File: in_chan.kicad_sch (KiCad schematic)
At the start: 8 parts, among them U5 MAX31910AUI+

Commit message: fix most errors/warnings
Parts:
- renumbered C33 to C45, C34 to C46, C35 to C47, C36 to C48, R6 to R10, R7 to R11, U5 to U8
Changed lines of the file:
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@@
   (symbol (lib_id "power:GNDPWR") (at 163.83 119.38 0)
     (in_bom yes) (on_board yes) (fields_autoplaced)
-    (property "Reference" "#PWR031" (id 0) (at 163.83 124.46 0)
+    (property "Reference" "#PWR051" (id 0) (at 163.83 124.46 0)
       (effects (font (size 1.27 1.27)) hide)
     )
@@
   (symbol (lib_id "Device:R") (at 163.83 113.03 180)
     (in_bom yes) (on_board yes)
-    (property "Reference" "R7" (id 0) (at 166.37 111.76 0)
+    (property "Reference" "R11" (id 0) (at 166.37 111.76 0)
       (effects (font (size 1.27 1.27)) (justify right))
     )
@@
   (symbol (lib_id "power:GNDPWR") (at 204.47 151.13 0) (mirror y)
     (in_bom yes) (on_board yes) (fields_autoplaced)
-    (property "Reference" "#PWR032" (id 0) (at 204.47 156.21 0)
+    (property "Reference" "#PWR052" (id 0) (at 204.47 156.21 0)
       (effects (font (size 1.27 1.27)) hide)
     )
@@
   (symbol (lib_id "power:GNDPWR") (at 243.84 66.04 0)
     (in_bom yes) (on_board yes) (fields_autoplaced)
-    (property "Reference" "#PWR034" (id 0) (at 243.84 71.12 0)
+    (property "Reference" "#PWR054" (id 0) (at 243.84 71.12 0)
       (effects (font (size 1.27 1.27)) hide)
     )
@@
   (symbol (lib_id "Device:C") (at 243.84 62.23 0)
     (in_bom yes) (on_board yes)
-    (property "Reference" "C36" (id 0) (at 247.65 60.9599 0)
+    (property "Reference" "C48" (id 0) (at 247.65 60.9599 0)
       (effects (font (size 1.27 1.27)) (justify left))
     )
@@
   (symbol (lib_id "Maxim industrial IO:MAX31910AUI+") (at 204.47 143.51 0)
     (in_bom yes) (on_board yes) (fields_autoplaced)
-    (property "Reference" "U5" (id 0) (at 238.76 143.51 0)
+    (property "Reference" "U8" (id 0) (at 238.76 143.51 0)
       (effects (font (size 1.524 1.524)) (justify left))
     )
@@
   (symbol (lib_id "Device:C") (at 187.96 147.32 0) (mirror y)
     (in_bom yes) (on_board yes)
-    (property "Reference" "C33" (id 0) (at 184.15 146.0499 0)
+    (property "Reference" "C45" (id 0) (at 184.15 146.0499 0)
       (effects (font (size 1.27 1.27)) (justify left))
     )
@@
   (symbol (lib_id "power:GNDPWR") (at 219.71 87.63 0)
     (in_bom yes) (on_board yes) (fields_autoplaced)
-    (property "Reference" "#PWR033" (id 0) (at 219.71 92.71 0)
+    (property "Reference" "#PWR053" (id 0) (at 219.71 92.71 0)
       (effects (font (size 1.27 1.27)) hide)
     )
@@
   (symbol (lib_id "Device:C") (at 232.41 62.23 0)
     (in_bom yes) (on_board yes)
-    (property "Reference" "C35" (id 0) (at 236.22 60.9599 0)
+    (property "Reference" "C47" (id 0) (at 236.22 60.9599 0)
       (effects (font (size 1.27 1.27)) (justify left))
     )
@@
   (symbol (lib_id "power:GNDPWR") (at 160.02 73.66 270)
     (in_bom yes) (on_board yes)
-    (property "Reference" "#PWR030" (id 0) (at 154.94 73.66 0)
+    (property "Reference" "#PWR050" (id 0) (at 154.94 73.66 0)
       (effects (font (size 1.27 1.27)) hide)
     )
@@
   (symbol (lib_id "Device:C") (at 196.85 147.32 0) (mirror y)
     (in_bom yes) (on_board yes)
-    (property "Reference" "C34" (id 0) (at 193.04 146.0499 0)
+    (property "Reference" "C46" (id 0) (at 193.04 146.0499 0)
       (effects (font (size 1.27 1.27)) (justify left))
     )
@@
   (symbol (lib_id "Num-IO:4816P-T01-103LF") (at 153.67 80.01 0)
     (in_bom yes) (on_board yes)
-    (property "Reference" "R6" (id 0) (at 160.02 77.47 0)
+    (property "Reference" "R10" (id 0) (at 160.02 77.47 0)
       (effects (font (size 1.524 1.524)))
     )
@@
   (symbol (lib_id "Maxim industrial IO:MAX31910AUI+") (at 168.91 58.42 0)
     (in_bom yes) (on_board yes) (fields_autoplaced)
-    (property "Reference" "U5" (id 0) (at 194.31 46.99 0)
-      (effects (font (size 1.524 1.524)))
-    )
+    (property "Reference" "U8" (id 0) (at 194.31 46.99 0)
+      (effects (font (size 1.524 1.524)))
+    )

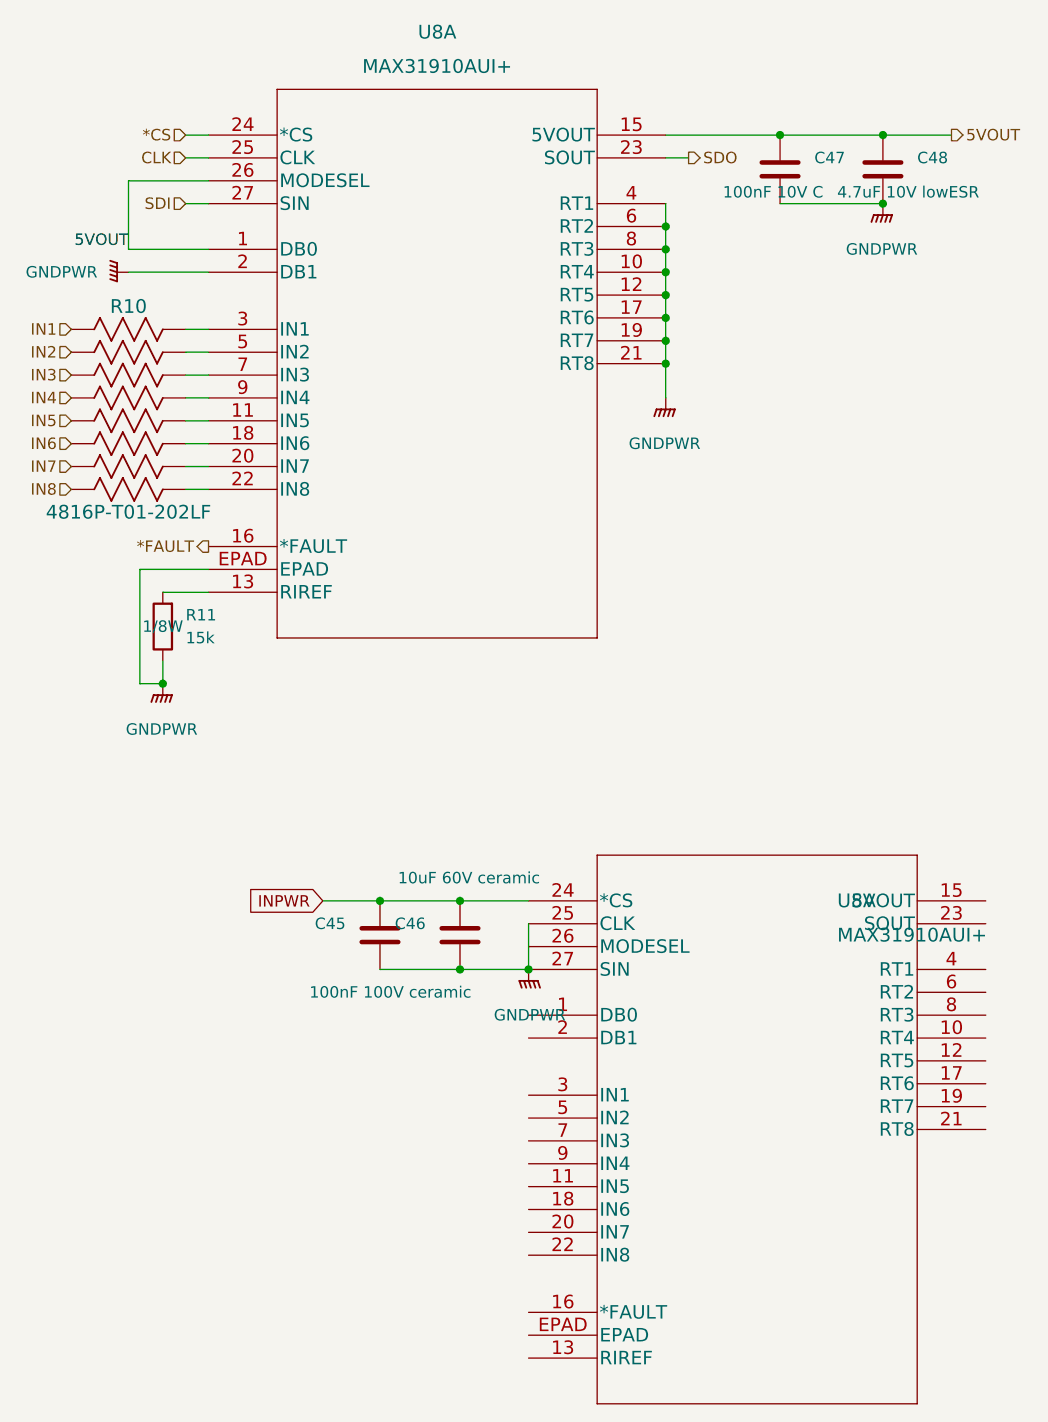
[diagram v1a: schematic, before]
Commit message: add KK connectors for power (check voltage or bypass)
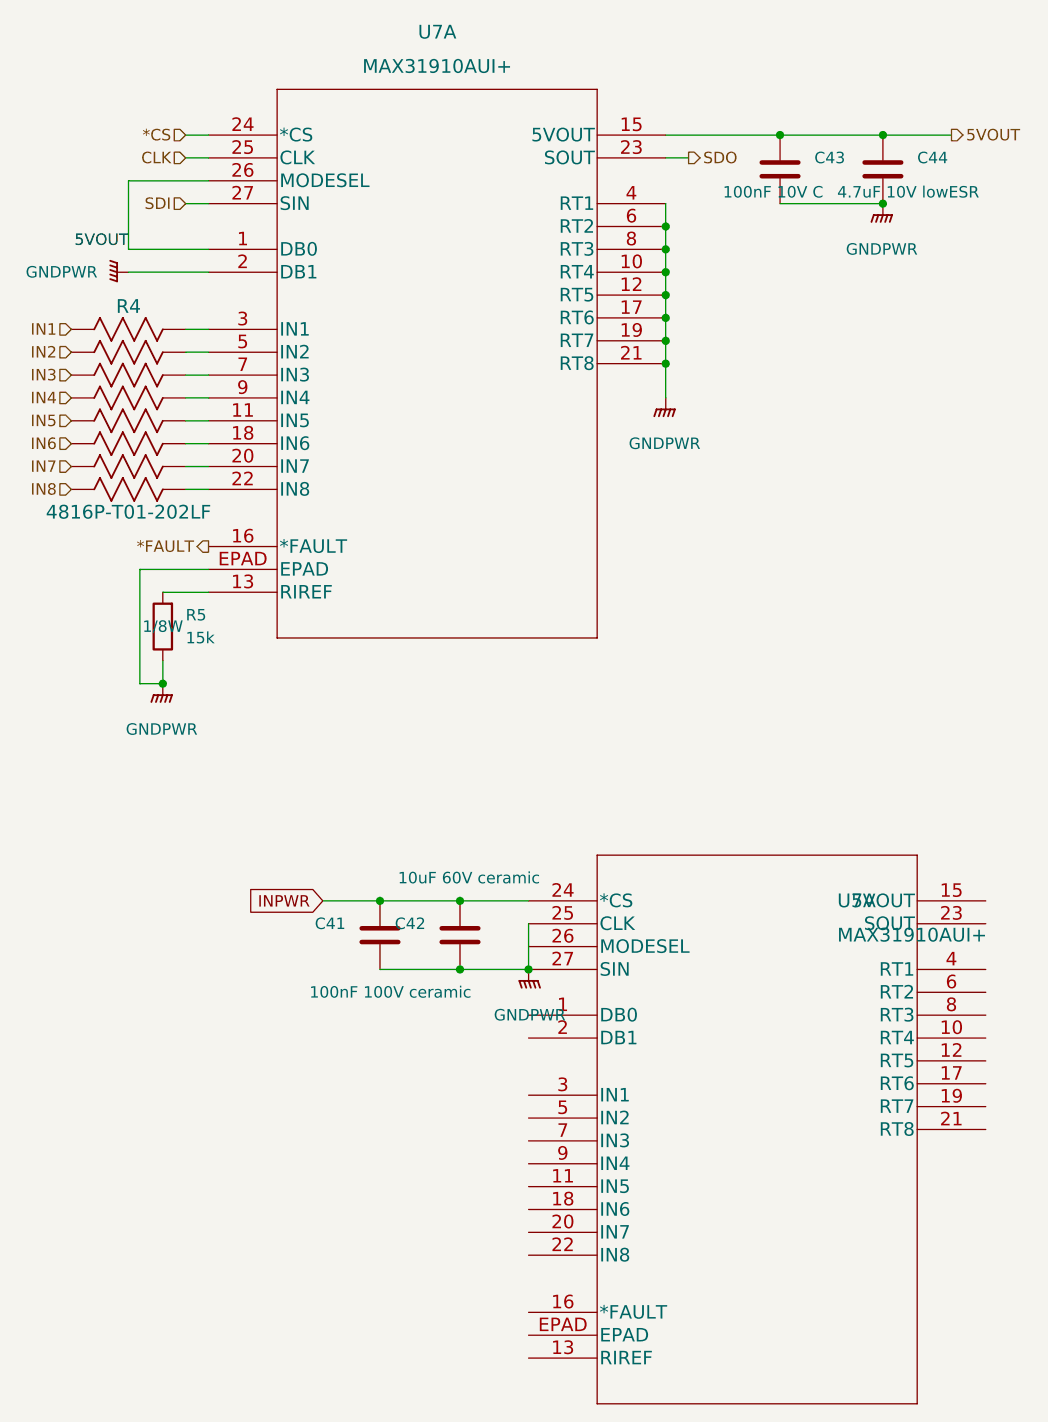
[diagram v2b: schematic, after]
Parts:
- renumbered C45 to C41, C46 to C42, C47 to C43, C48 to C44, R10 to R4, R11 to R5, U8 to U7
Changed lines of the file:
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@@
   (symbol (lib_id "Device:R") (at 163.83 113.03 180)
     (in_bom yes) (on_board yes)
-    (property "Reference" "R11" (id 0) (at 166.37 111.76 0)
+    (property "Reference" "R5" (id 0) (at 166.37 111.76 0)
       (effects (font (size 1.27 1.27)) (justify right))
     )
@@
   (symbol (lib_id "Device:C") (at 243.84 62.23 0)
     (in_bom yes) (on_board yes)
-    (property "Reference" "C48" (id 0) (at 247.65 60.9599 0)
+    (property "Reference" "C44" (id 0) (at 247.65 60.9599 0)
       (effects (font (size 1.27 1.27)) (justify left))
     )
@@
   (symbol (lib_id "Maxim industrial IO:MAX31910AUI+") (at 204.47 143.51 0)
     (in_bom yes) (on_board yes) (fields_autoplaced)
-    (property "Reference" "U8" (id 0) (at 238.76 143.51 0)
+    (property "Reference" "U7" (id 0) (at 238.76 143.51 0)
       (effects (font (size 1.524 1.524)) (justify left))
     )
@@
   (symbol (lib_id "Device:C") (at 187.96 147.32 0) (mirror y)
     (in_bom yes) (on_board yes)
-    (property "Reference" "C45" (id 0) (at 184.15 146.0499 0)
+    (property "Reference" "C41" (id 0) (at 184.15 146.0499 0)
       (effects (font (size 1.27 1.27)) (justify left))
     )
@@
   (symbol (lib_id "Device:C") (at 232.41 62.23 0)
     (in_bom yes) (on_board yes)
-    (property "Reference" "C47" (id 0) (at 236.22 60.9599 0)
+    (property "Reference" "C43" (id 0) (at 236.22 60.9599 0)
       (effects (font (size 1.27 1.27)) (justify left))
     )
@@
   (symbol (lib_id "Device:C") (at 196.85 147.32 0) (mirror y)
     (in_bom yes) (on_board yes)
-    (property "Reference" "C46" (id 0) (at 193.04 146.0499 0)
+    (property "Reference" "C42" (id 0) (at 193.04 146.0499 0)
       (effects (font (size 1.27 1.27)) (justify left))
     )
@@
   (symbol (lib_id "Num-IO:4816P-T01-103LF") (at 153.67 80.01 0)
     (in_bom yes) (on_board yes)
-    (property "Reference" "R10" (id 0) (at 160.02 77.47 0)
+    (property "Reference" "R4" (id 0) (at 160.02 77.47 0)
       (effects (font (size 1.524 1.524)))
     )
@@
   (symbol (lib_id "Maxim industrial IO:MAX31910AUI+") (at 168.91 58.42 0)
     (in_bom yes) (on_board yes) (fields_autoplaced)
-    (property "Reference" "U8" (id 0) (at 194.31 46.99 0)
+    (property "Reference" "U7" (id 0) (at 194.31 46.99 0)
       (effects (font (size 1.524 1.524)))
     )

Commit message: add resistances for bypassing the isolator
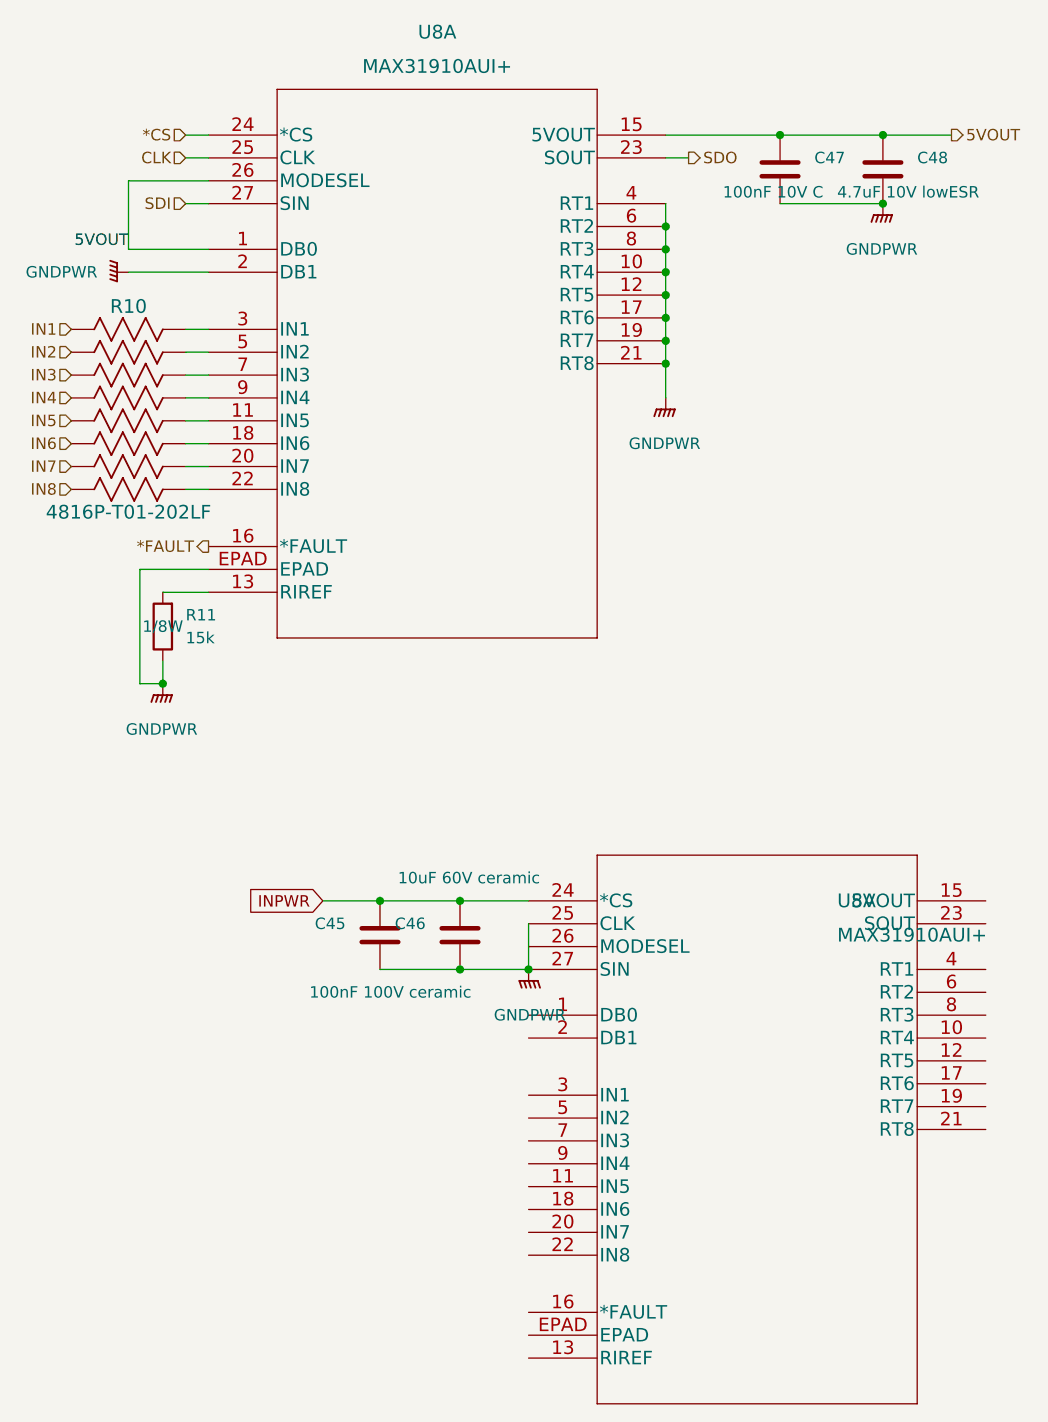
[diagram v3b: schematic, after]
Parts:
- renumbered C41 to C45, C42 to C46, C43 to C47, C44 to C48, R4 to R10, R5 to R11, U7 to U8
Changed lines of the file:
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@@
   (symbol (lib_id "Device:R") (at 163.83 113.03 180)
     (in_bom yes) (on_board yes)
-    (property "Reference" "R5" (id 0) (at 166.37 111.76 0)
+    (property "Reference" "R11" (id 0) (at 166.37 111.76 0)
       (effects (font (size 1.27 1.27)) (justify right))
     )
@@
   (symbol (lib_id "Device:C") (at 243.84 62.23 0)
     (in_bom yes) (on_board yes)
-    (property "Reference" "C44" (id 0) (at 247.65 60.9599 0)
+    (property "Reference" "C48" (id 0) (at 247.65 60.9599 0)
       (effects (font (size 1.27 1.27)) (justify left))
     )
@@
   (symbol (lib_id "Maxim industrial IO:MAX31910AUI+") (at 204.47 143.51 0)
     (in_bom yes) (on_board yes) (fields_autoplaced)
-    (property "Reference" "U7" (id 0) (at 238.76 143.51 0)
+    (property "Reference" "U8" (id 0) (at 238.76 143.51 0)
       (effects (font (size 1.524 1.524)) (justify left))
     )
@@
   (symbol (lib_id "Device:C") (at 187.96 147.32 0) (mirror y)
     (in_bom yes) (on_board yes)
-    (property "Reference" "C41" (id 0) (at 184.15 146.0499 0)
+    (property "Reference" "C45" (id 0) (at 184.15 146.0499 0)
       (effects (font (size 1.27 1.27)) (justify left))
     )
@@
   (symbol (lib_id "Device:C") (at 232.41 62.23 0)
     (in_bom yes) (on_board yes)
-    (property "Reference" "C43" (id 0) (at 236.22 60.9599 0)
+    (property "Reference" "C47" (id 0) (at 236.22 60.9599 0)
       (effects (font (size 1.27 1.27)) (justify left))
     )
@@
   (symbol (lib_id "Device:C") (at 196.85 147.32 0) (mirror y)
     (in_bom yes) (on_board yes)
-    (property "Reference" "C42" (id 0) (at 193.04 146.0499 0)
+    (property "Reference" "C46" (id 0) (at 193.04 146.0499 0)
       (effects (font (size 1.27 1.27)) (justify left))
     )
@@
   (symbol (lib_id "Num-IO:4816P-T01-103LF") (at 153.67 80.01 0)
     (in_bom yes) (on_board yes)
-    (property "Reference" "R4" (id 0) (at 160.02 77.47 0)
+    (property "Reference" "R10" (id 0) (at 160.02 77.47 0)
       (effects (font (size 1.524 1.524)))
     )
@@
   (symbol (lib_id "Maxim industrial IO:MAX31910AUI+") (at 168.91 58.42 0)
     (in_bom yes) (on_board yes) (fields_autoplaced)
-    (property "Reference" "U7" (id 0) (at 194.31 46.99 0)
+    (property "Reference" "U8" (id 0) (at 194.31 46.99 0)
       (effects (font (size 1.524 1.524)))
     )

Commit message: add condo for MPG isolator + small rerouting pair diff
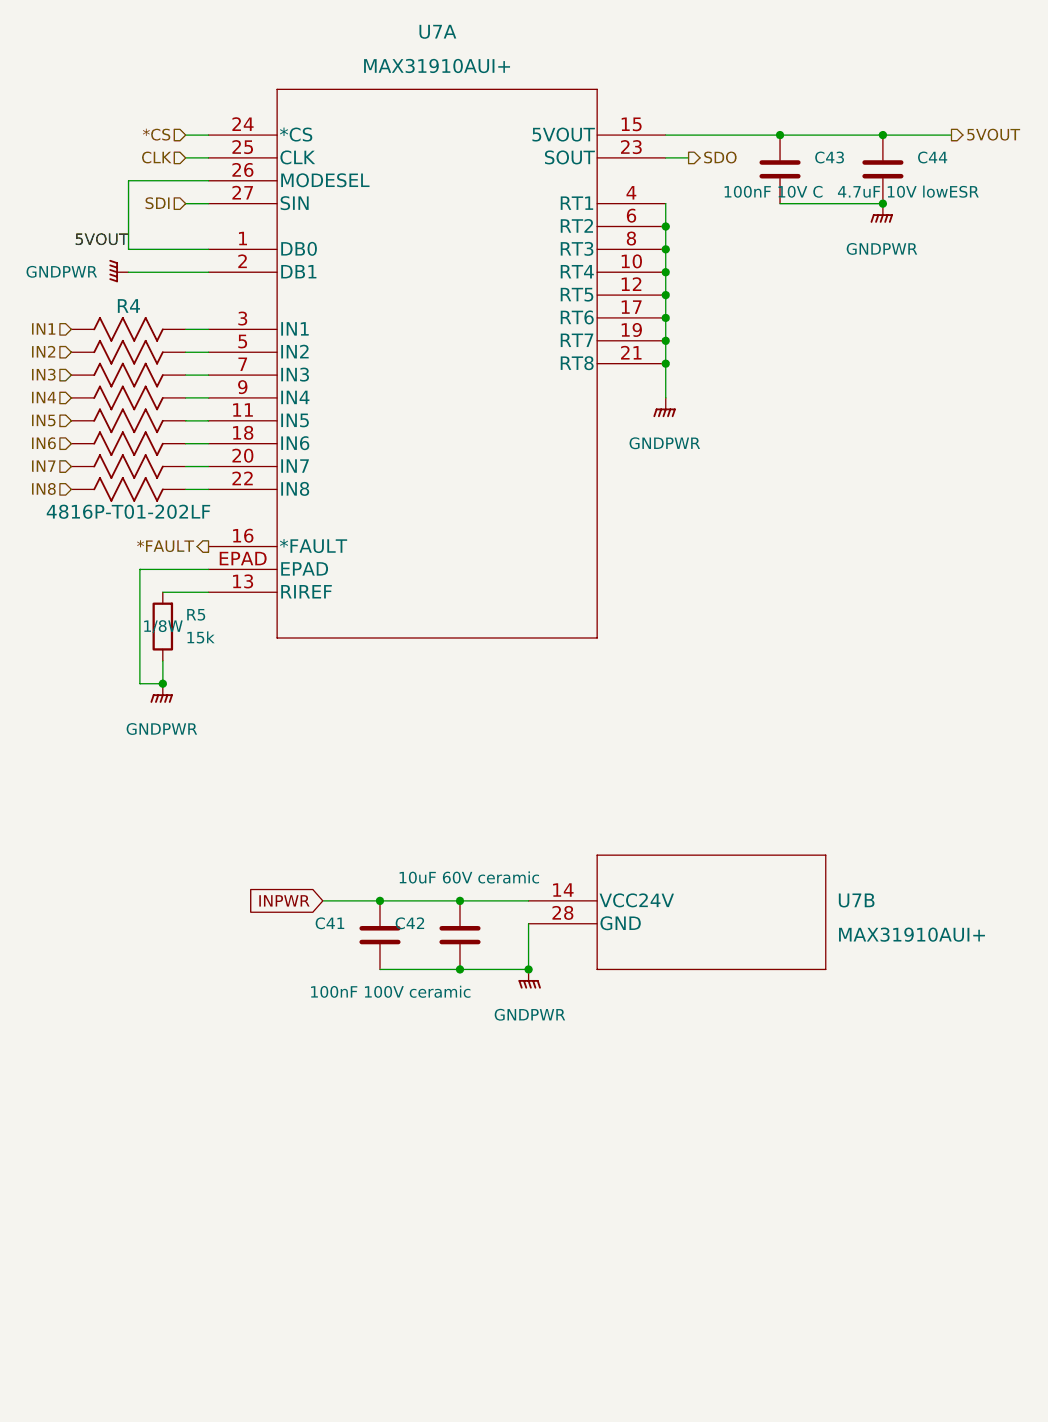
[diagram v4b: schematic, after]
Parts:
- renumbered C45 to C41, C46 to C42, C47 to C43, C48 to C44, R10 to R4, R11 to R5, U8 to U7
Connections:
- net GNDPWR: now also U7.28 (GND); no longer U7.25 (CLK), U7.27 (SIN)
- net INPWR: now also U7.14 (VCC24V); no longer U7.24 (*CS)
